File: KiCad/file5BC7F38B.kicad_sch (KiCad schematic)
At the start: 78 parts, among them J301 DB9_Female, J302 Conn_01x06, J303 DB9_Male, J304 Conn_01x10, J305 Conn_01x02, J306 Conn_01x02, J307 Conn_01x02, J308 Conn_01x02, P301 ISP/PDI, P302 Thru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

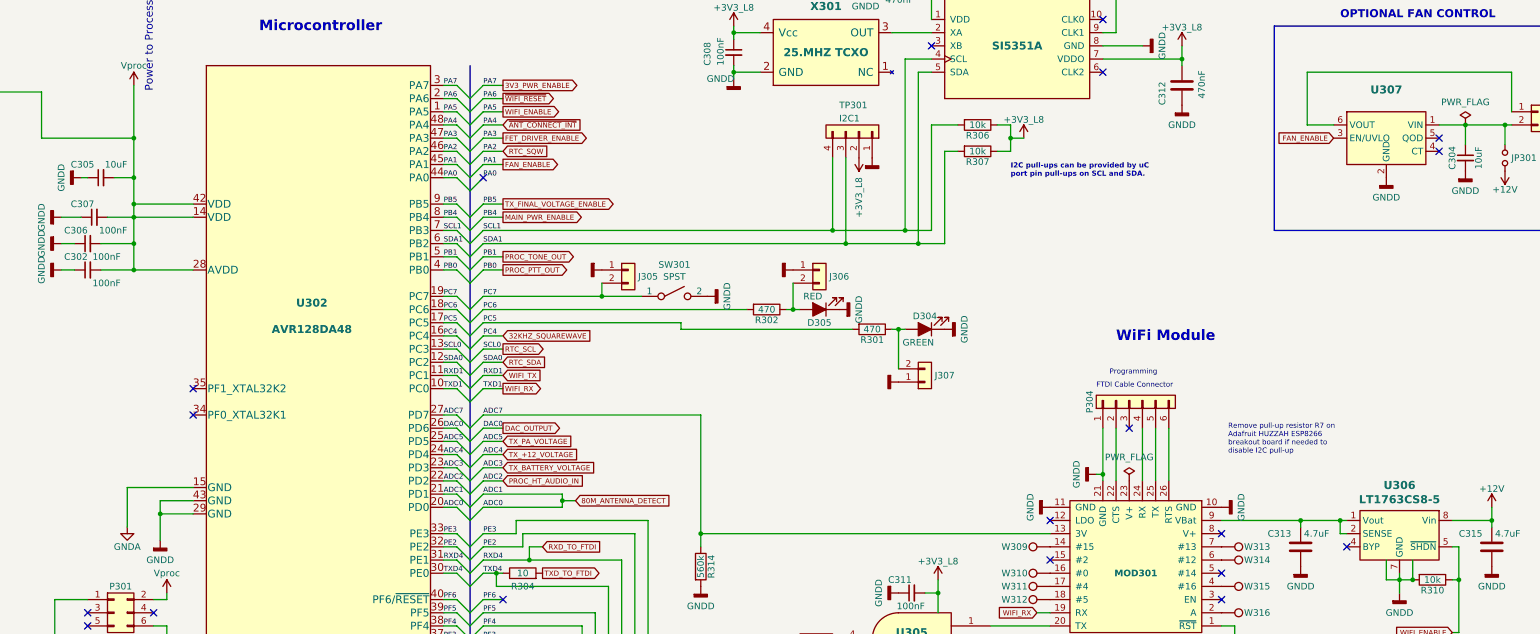
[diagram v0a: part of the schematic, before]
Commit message: KiCad Updates
o Fixes for problems found during first board build
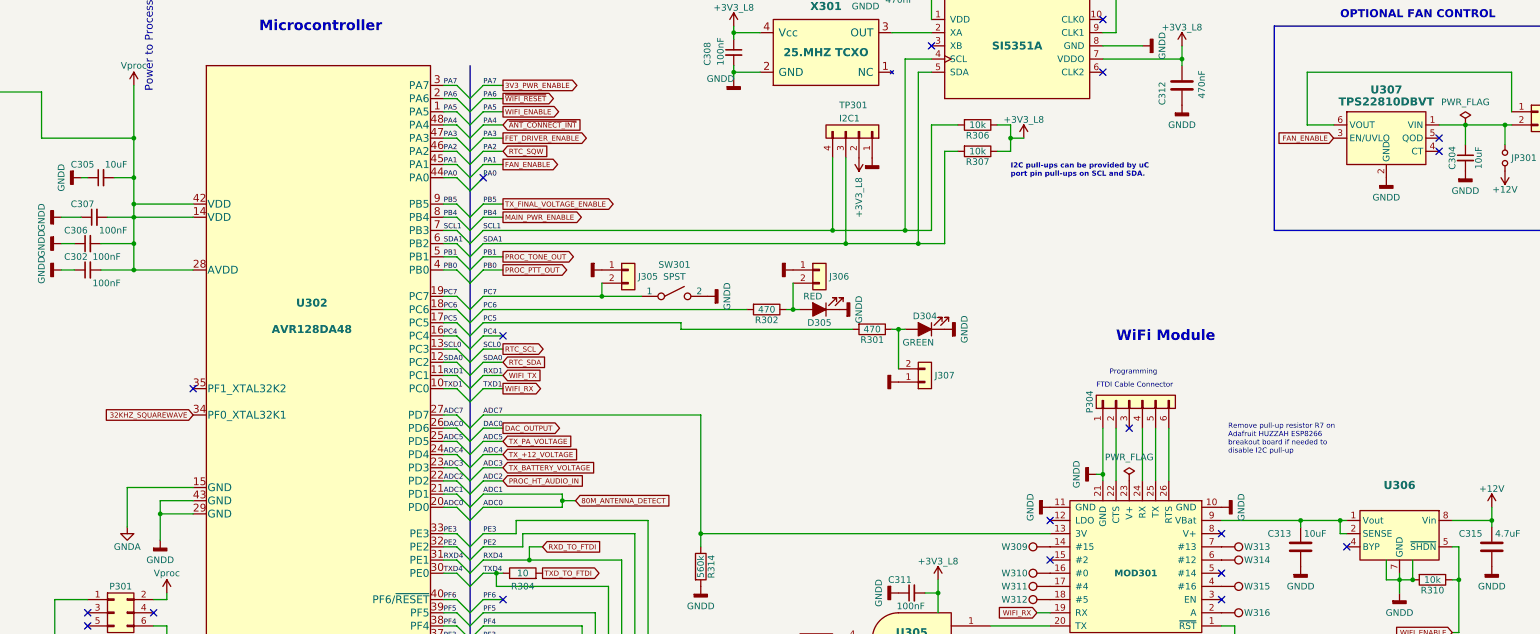
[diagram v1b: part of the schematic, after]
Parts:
- C313: value 4.7uF -> 10uF; Digi-Key Part No. 587-2990-1-ND -> 490-5523-1-ND; LCSC Part Number C162420 -> C84416; Link <a href="https://www.digikey.com/products/en?keywords=587-2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 -> <a href="https://www.digikey.com/products/en?keywords=490-5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; Manufacturer Taiyo Yuden -> Murata Electronics; Manufacturer PN TMK212AB7475KG-T -> GRM21BR61E106KA73L
- U306: value LT1763CS8-5 -> (none); footprint Housings_SOIC:SOIC-8_3.9x4.9mm_Pitch1.27mm -> (none); LCSC Part Number C193629 -> C117275
- U307: value (none) -> TPS22810DBVT; footprint (none) -> TO_SOT_Packages_SMD:SOT-23-6
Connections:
- net 32KHZ_SQUAREWAVE: now also U302.34 (PF0_XTAL32K1); no longer U302.16 (PC4)
- new net PC4: U302.16 (PC4)
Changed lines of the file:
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@@
   (no_connect (at 144.78 233.68))
   (no_connect (at 142.24 146.05))
-  (no_connect (at 142.24 151.13))
   (no_connect (at 382.27 100.33))
   (no_connect (at 91.44 92.71))
@@
   (no_connect (at 90.17 55.88))
   (no_connect (at 201.93 186.69))
+  (no_connect (at 201.93 135.89))
   (no_connect (at 78.74 222.25))
   (no_connect (at 340.36 181.61))
@@
     )
   )
-  (global_label "32KHZ_SQUAREWAVE" (shape input) (at 201.93 135.89 0) (fields_autoplaced)
-    (effects (font (size 0.9906 0.9906)) (justify left))
-    (property "Intersheet References" "${INTERSHEET_REFS}" (id 0) (at 0 0 0)
+  (global_label "32KHZ_SQUAREWAVE" (shape input) (at 142.24 151.13 180) (fields_autoplaced)
+    (effects (font (size 0.9906 0.9906)) (justify right))
+    (property "Intersheet References" "${INTERSHEET_REFS}" (id 0) (at 344.17 287.02 0)
       (effects (font (size 1.27 1.27)) hide)
     )
@@
       (effects (font (size 1.27 1.27)) (justify left))
     )
-    (property "Value" "4.7uF" (id 1) (at 356.235 173.99 0)
+    (property "Value" "10uF" (id 1) (at 356.235 173.99 0)
       (effects (font (size 1.27 1.27)) (justify left))
     )
@@
       (effects (font (size 1.27 1.27)) hide)
     )
-    (property "Digi-Key Part No." "587-2990-1-ND" (id 4) (at 355.6 176.53 0)
+    (property "Digi-Key Part No." "490-5523-1-ND" (id 4) (at 355.6 176.53 0)
       (effects (font (size 1.27 1.27)) hide)
     )
-    (property "Link" "<a href=\"https://www.digikey.com/products/en?keywords=587-2990-1-ND\">Link</a>" (id 5) (at 355.6 176.53 0)
+    (property "Link" "<a href=\"https://www.digikey.com/products/en?keywords=490-5523-1-ND\">Link</a>" (id 5) (at 355.6 176.53 0)
       (effects (font (size 1.524 1.524)) hide)
     )
-    (property "Manufacturer" "Taiyo Yuden" (id 6) (at 355.6 176.53 0)
+    (property "Manufacturer" "Murata Electronics" (id 6) (at 355.6 176.53 0)
       (effects (font (size 1.27 1.27)) hide)
     )
-    (property "Manufacturer PN" "TMK212AB7475KG-T" (id 7) (at 355.6 176.53 0)
+    (property "Manufacturer PN" "GRM21BR61E106KA73L" (id 7) (at 355.6 176.53 0)
       (effects (font (size 1.27 1.27)) hide)
     )
-    (property "Description" "CAP CER 4.7UF 25V X7R 0805" (id 8) (at 355.6 176.53 0)
+    (property "Description" "CAP CER 10UF 25V X5R 0805" (id 8) (at 355.6 176.53 0)
       (effects (font (size 1.27 1.27)) hide)
     )
-    (property "LCSC Part Number" "C162420" (id 9) (at 355.6 176.53 0)
+    (property "LCSC Part Number" "C84416" (id 9) (at 355.6 176.53 0)
       (effects (font (size 1.27 1.27)) hide)
     )
@@
       (effects (font (size 1.5494 1.5494) bold))
     )
-    (property "Value" "LT1763CS8-5" (id 1) (at 374.65 167.4114 0)
+    (property "Value" "" (id 1) (at 374.65 167.4114 0)
       (effects (font (size 1.5494 1.5494) bold))
     )
-    (property "Footprint" "Housings_SOIC:SOIC-8_3.9x4.9mm_Pitch1.27mm" (id 2) (at 374.015 180.34 0)
+    (property "Footprint" "" (id 2) (at 374.015 180.34 0)
       (effects (font (size 1.27 1.27) italic) (justify left) hide)
     )
@@
       (effects (font (size 1.27 1.27)) hide)
     )
-    (property "LCSC Part Number" "C193629" (id 9) (at 374.65 173.99 0)
+    (property "LCSC Part Number" "C117275" (id 9) (at 374.65 173.99 0)
       (effects (font (size 1.27 1.27)) hide)
     )
@@
       (effects (font (size 1.5494 1.5494) bold))
     )
-    (property "Value" "" (id 1) (at 372.11 90.7796 0)
+    (property "Value" "TPS22810DBVT" (id 1) (at 372.11 90.7796 0)
       (effects (font (size 1.5494 1.5494) bold))
     )
-    (property "Footprint" "" (id 2) (at 372.11 115.57 0)
+    (property "Footprint" "TO_SOT_Packages_SMD:SOT-23-6" (id 2) (at 372.11 115.57 0)
       (effects (font (size 1.27 1.27)) hide)
     )

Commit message: Updates
Schematic
Fixes to events.html
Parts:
- added JP?: Jumper_NO_Small, Wire_Connections_Bridges:Solder-Jumper-NO-SMD-Pad_Small, symbol FlexFox80-rescue:Jumper_NO_Small-Device
- J302: value Conn_01x06 -> (none); footprint Pin_Headers:Pin_Header_Angled_1x06 -> (none)
- J304: value Conn_01x10 -> (none); footprint Pin_Headers:Pin_Header_Straight_1x10 -> (none)
- J305, J306, J307: value Conn_01x02 -> (none); footprint Pin_Headers:Pin_Header_Straight_1x02 -> (none)
- J308: value Conn_01x02 -> (none); footprint Pin_Headers:Pin_Header_Straight_1x02 -> (none); symbol Connector_Generic:Conn_01x02 -> Connector_Generic:Conn_01x03
- P304: value Header -> (none); footprint Pin_Headers:Pin_Header_Straight_1x06 -> (none)
- TP301: value I2C1 -> (none); footprint Pin_Headers:Pin_Header_Straight_1x04 -> (none)
- TP302: value I2C0 -> (none); footprint Pin_Headers:Pin_Header_Straight_1x04 -> (none)
- U306: value (none) -> LT1763CS8-5; footprint (none) -> Housings_SOIC:SOIC-8_3.9x4.9mm_Pitch1.27mm
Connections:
- net GND: now also J308.1 (Pin_1)
- net at C304.1, JP301.1, U307.1 (VIN): now also J308.3 (Pin_3), JP?.1; no longer J308.2 (Pin_2)
- net at U307.6 (VOUT): now also J308.2 (Pin_2); no longer J308.1 (Pin_1)
- new net Battery: JP?.2
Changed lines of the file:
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@@
   (junction (at 284.48 67.31) (diameter 0) (color 0 0 0 0)
   )
+  (junction (at 392.43 95.25) (diameter 0) (color 0 0 0 0)
+  )
   (junction (at 377.19 182.88) (diameter 0) (color 0 0 0 0)
   )
@@
     (stroke (width 0) (type default) (color 0 0 0 0))
   )
-  (wire (pts (xy 387.35 95.25) (xy 394.97 95.25))
+  (wire (pts (xy 387.35 95.25) (xy 392.43 95.25))
     (stroke (width 0) (type default) (color 0 0 0 0))
   )
@@
     (stroke (width 0) (type default) (color 0 0 0 0))
   )
+  (wire (pts (xy 392.43 95.25) (xy 392.43 99.06))
+    (stroke (width 0) (type default) (color 0 0 0 0))
+  )
   (wire (pts (xy 198.12 168.91) (xy 213.36 168.91))
     (stroke (width 0) (type default) (color 0 0 0 0))
@@
     (stroke (width 0) (type default) (color 0 0 0 0))
   )
-  (wire (pts (xy 396.24 85.09) (xy 396.24 92.71))
+  (wire (pts (xy 392.43 85.09) (xy 392.43 92.71))
     (stroke (width 0) (type default) (color 0 0 0 0))
   )
@@
     (stroke (width 0) (type default) (color 0 0 0 0))
   )
+  (wire (pts (xy 392.43 95.25) (xy 394.97 95.25))
+    (stroke (width 0) (type default) (color 0 0 0 0))
+  )
   (wire (pts (xy 224.79 179.07) (xy 224.79 217.17))
     (stroke (width 0) (type default) (color 0 0 0 0))
@@
     (stroke (width 0) (type default) (color 0 0 0 0))
   )
+  (wire (pts (xy 392.43 104.14) (xy 392.43 111.76))
+    (stroke (width 0) (type default) (color 0 0 0 0))
+  )
+  (wire (pts (xy 396.24 85.09) (xy 396.24 90.17))
+    (stroke (width 0) (type default) (color 0 0 0 0))
+  )
   (wire (pts (xy 58.42 154.94) (xy 58.42 156.21))
     (stroke (width 0) (type default) (color 0 0 0 0))
@@
     (stroke (width 0) (type default) (color 0 0 0 0))
   )
-  (wire (pts (xy 356.87 85.09) (xy 396.24 85.09))
+  (wire (pts (xy 356.87 85.09) (xy 392.43 85.09))
     (stroke (width 0) (type default) (color 0 0 0 0))
   )
@@
     (stroke (width 0) (type default) (color 0 0 0 0))
   )
+  (wire (pts (xy 392.43 92.71) (xy 396.24 92.71))
+    (stroke (width 0) (type default) (color 0 0 0 0))
+  )
   (wire (pts (xy 127 105.41) (xy 130.81 105.41))
     (stroke (width 0) (type default) (color 0 0 0 0))
@@
     )
   )
+  (global_label "Battery" (shape input) (at 392.43 111.76 180) (fields_autoplaced)
+    (effects (font (size 0.9906 0.9906)) (justify right))
+    (property "Intersheet References" "${INTERSHEET_REFS}" (id 0) (at 385.3813 111.6981 0)
+      (effects (font (size 0.9906 0.9906)) (justify right) hide)
+    )
+  )
   (global_label "RXD_TO_FTDI" (shape input) (at 209.55 176.53 0) (fields_autoplaced)
     (effects (font (size 0.9906 0.9906)) (justify left))
@@
     (in_bom yes) (on_board yes)
     (property "Reference" "P304" (id 0) (at 314.96 148.59 0))
-    (property "Value" "Header" (id 1) (at 323.85 146.05 90)
+    (property "Value" "" (id 1) (at 323.85 146.05 90)
       (effects (font (size 1.27 1.27)) hide)
     )
-    (property "Footprint" "Pin_Headers:Pin_Header_Straight_1x06" (id 2) (at 323.85 148.59 0)
+    (property "Footprint" "" (id 2) (at 323.85 148.59 0)
       (effects (font (size 1.27 1.27)) hide)
     )
@@
       (effects (font (size 1.27 1.27)) (justify left))
     )
-    (property "Value" "I2C0" (id 1) (at 77.47 143.51 90)
+    (property "Value" "" (id 1) (at 77.47 143.51 90)
       (effects (font (size 1.27 1.27)) (justify left))
     )
-    (property "Footprint" "Pin_Headers:Pin_Header_Straight_1x04" (id 2) (at 81.28 146.05 0)
+    (property "Footprint" "" (id 2) (at 81.28 146.05 0)
       (effects (font (size 1.27 1.27)) hide)
     )
@@
       (effects (font (size 1.27 1.27)) (justify left))
     )
-    (property "Value" "Conn_01x06" (id 1) (at 159.512 245.0846 0)
+    (property "Value" "" (id 1) (at 159.512 245.0846 0)
       (effects (font (size 1.27 1.27)) (justify left))
     )
-    (property "Footprint" "Pin_Headers:Pin_Header_Angled_1x06" (id 2) (at 157.48 242.57 0)
+    (property "Footprint" "" (id 2) (at 157.48 242.57 0)
       (effects (font (size 1.27 1.27)) hide)
     )
@@
       (effects (font (size 1.5494 1.5494) bold))
     )
-    (property "Value" "" (id 1) (at 374.65 167.4114 0)
+    (property "Value" "LT1763CS8-5" (id 1) (at 374.65 167.4114 0)
       (effects (font (size 1.5494 1.5494) bold))
     )
-    (property "Footprint" "" (id 2) (at 374.015 180.34 0)
+    (property "Footprint" "Housings_SOIC:SOIC-8_3.9x4.9mm_Pitch1.27mm" (id 2) (at 374.015 180.34 0)
       (effects (font (size 1.27 1.27) italic) (justify left) hide)
     )
@@
       (effects (font (size 1.27 1.27)) (justify left))
     )
-    (property "Value" "I2C1" (id 1) (at 266.7 93.98 90)
+    (property "Value" "" (id 1) (at 266.7 93.98 90)
       (effects (font (size 1.27 1.27)) (justify left))
     )
-    (property "Footprint" "Pin_Headers:Pin_Header_Straight_1x04" (id 2) (at 270.51 96.52 0)
+    (property "Footprint" "" (id 2) (at 270.51 96.52 0)
       (effects (font (size 1.27 1.27)) hide)
     )
@@
     (in_bom yes) (on_board yes)
     (property "Reference" "J304" (id 0) (at 218.44 227.33 90))
-    (property "Value" "Conn_01x10" (id 1) (at 233.2736 220.1672 0)
+    (property "Value" "" (id 1) (at 233.2736 220.1672 0)
       (effects (font (size 1.27 1.27)) hide)
     )
-    (property "Footprint" "Pin_Headers:Pin_Header_Straight_1x10" (id 2) (at 217.17 222.25 0)
+    (property "Footprint" "" (id 2) (at 217.17 222.25 0)
       (effects (font (size 1.27 1.27)) hide)
     )
@@
     (pin "1")
   )
-  (symbol (lib_id "Connector_Generic:Conn_01x02") (at 401.32 92.71 0) (unit 1)
+  (symbol (lib_id "Connector_Generic:Conn_01x03") (at 401.32 92.71 0) (unit 1)
     (in_bom yes) (on_board yes)
     (property "Reference" "J308" (id 0) (at 405.13 93.98 0))
-    (property "Value" "Conn_01x02" (id 1) (at 399.2372 98.6536 0)
+    (property "Value" "" (id 1) (at 399.2372 98.6536 0)
       (effects (font (size 1.27 1.27)) hide)
     )
-    (property "Footprint" "Pin_Headers:Pin_Header_Straight_1x02" (id 2) (at 401.32 92.71 0)
+    (property "Footprint" "" (id 2) (at 401.32 92.71 0)
       (effects (font (size 1.27 1.27)) hide)
     )
-    (property "Datasheet" "" (id 3) (at 401.32 92.71 0)
+    (property "Datasheet" "~" (id 3) (at 401.32 92.71 0)
       (effects (font (size 1.27 1.27)) hide)
     )
@@
     (pin "1")
     (pin "2")
+    (pin "3")
   )
   (symbol (lib_id "Device:C_Small") (at 387.35 101.6 0) (unit 1)
@@
     (in_bom yes) (on_board yes)
     (property "Reference" "J307" (id 0) (at 287.02 143.51 0))
-    (property "Value" "Conn_01x02" (id 1) (at 281.1272 138.8364 0)
+    (property "Value" "" (id 1) (at 281.1272 138.8364 0)
       (effects (font (size 1.27 1.27)) hide)
     )
-    (property "Footprint" "Pin_Headers:Pin_Header_Straight_1x02" (id 2) (at 283.21 144.78 0)
+    (property "Footprint" "" (id 2) (at 283.21 144.78 0)
       (effects (font (size 1.27 1.27)) hide)
     )
@@
     (in_bom yes) (on_board yes)
     (property "Reference" "J306" (id 0) (at 266.7 124.46 0))
-    (property "Value" "Conn_01x02" (id 1) (at 260.8072 129.1336 0)
+    (property "Value" "" (id 1) (at 260.8072 129.1336 0)
       (effects (font (size 1.27 1.27)) hide)
     )
-    (property "Footprint" "Pin_Headers:Pin_Header_Straight_1x02" (id 2) (at 262.89 123.19 0)
+    (property "Footprint" "" (id 2) (at 262.89 123.19 0)
       (effects (font (size 1.27 1.27)) hide)
     )
@@
     (in_bom yes) (on_board yes)
     (property "Reference" "J305" (id 0) (at 229.87 124.46 0))
-    (property "Value" "Conn_01x02" (id 1) (at 223.9772 129.1336 0)
+    (property "Value" "" (id 1) (at 223.9772 129.1336 0)
       (effects (font (size 1.27 1.27)) hide)
     )
-    (property "Footprint" "Pin_Headers:Pin_Header_Straight_1x02" (id 2) (at 226.06 123.19 0)
+    (property "Footprint" "" (id 2) (at 226.06 123.19 0)
       (effects (font (size 1.27 1.27)) hide)
     )
@@
     (pin "1")
   )
+  (symbol (lib_id "FlexFox80-rescue:Jumper_NO_Small-Device") (at 392.43 101.6 270) (unit 1)
+    (in_bom yes) (on_board yes)
+    (property "Reference" "JP?" (id 0) (at 387.35 97.79 90)
+      (effects (font (size 1.27 1.27)) (justify left))
+    )
+    (property "Value" "Jumper_NO_Small" (id 1) (at 393.6492 102.743 90)
+      (effects (font (size 1.27 1.27)) (justify left) hide)
+    )
+    (property "Footprint" "Wire_Connections_Bridges:Solder-Jumper-NO-SMD-Pad_Small" (id 2) (at 392.43 101.6 0)
+      (effects (font (size 1.27 1.27)) hide)
+    )
+    (property "Datasheet" "" (id 3) (at 392.43 101.6 0)
+      (effects (font (size 1.27 1.27)) hide)
+    )
+    (property "Digi-Key Part No." "np" (id 4) (at 392.43 101.6 0)
+      (effects (font (size 1.27 1.27)) hide)
+    )
+    (property "Link" "np" (id 5) (at 392.43 101.6 0)
+      (effects (font (size 1.27 1.27)) hide)
+    )
+    (property "Manufacturer" "np" (id 6) (at 392.43 101.6 0)
+      (effects (font (size 1.27 1.27)) hide)
+    )
+    (pin "1")
+    (pin "2")
+  )
+  (symbol (lib_id "power:GNDD") (at 396.24 85.09 180) (unit 1)
+    (in_bom yes) (on_board yes)
+    (property "Reference" "#PWR?" (id 0) (at 396.24 78.74 0)
+      (effects (font (size 1.27 1.27)) hide)
+    )
+    (property "Value" "GNDD" (id 1) (at 396.24 81.28 0)
+      (effects (font (size 1.27 1.27)) hide)
+    )
+    (property "Footprint" "" (id 2) (at 396.24 85.09 0))
+    (property "Datasheet" "" (id 3) (at 396.24 85.09 0))
+    (pin "1")
+  )
